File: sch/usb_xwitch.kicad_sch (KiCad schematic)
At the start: 62 parts, among them J1 USB3_A, J2 USB3_A, J3 USB3_A, J4 USB3_A, J5 USB3_A, J6 USB3_A, J7 USB3_A, J8 Conn_02x05_Odd_Even, J9 Conn_02x03_Odd_Even, K1 J104D2C3VDC.15S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

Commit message: updated 3d model and pcb, sch finalize
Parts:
- added D8: VS-10BQ015, Diode_SMD:D_SMB_Handsoldering, symbol Diode:Z2SMBxxx
- added Q3: 2N7002P, Package_TO_SOT_SMD:SOT-23, symbol Transistor_FET:2N7002
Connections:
- net SW-B is gone; now on net REL-B: TP7.1, U1.27 (GPIO21)
- net +5V: now also K3.A1, D8.1 (K)
- net GND: now also K3.11, Q3.2 (S)
- net REL-B: no longer TP6.1, U1.26 (GPIO20)
- net VBUS2: now reaches J5.1 (VBUS), K2.22
- net VBUS2: now also R11.1
- net at J6.1 (VBUS): now also K3.21
- net at J6.2 (D-): now also J7.2 (D-)
- net at J6.3 (D+): now also J7.3 (D+)
- net at J6.5 (SSRX-): now also J7.5 (SSRX-)
- net at J6.6 (SSRX+): now also J7.6 (SSRX+)
- net at J6.8 (SSTX-): now also J7.8 (SSTX-)
- net at J6.9 (SSTX+): now also J7.9 (SSTX+)
- net VBUS3: now reaches J7.1 (VBUS)
- net VBUS3: now also K3.22, R12.1
- net at J7.10 (SHIELD), J7.4 (GND), J7.7 (DRAIN): now also K3.12
- net RL3: now reaches K3.A2
- net RL3: now also D8.2 (A), Q3.3 (D)
- new net REL-C: Q3.1 (G), TP6.1, U1.26 (GPIO20)
- no-connect marks 26 -> 28
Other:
- moved on the sheet: C9, D1, D2, D3, D4, D5, D6, D7, J8, J9, JP1, JP2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

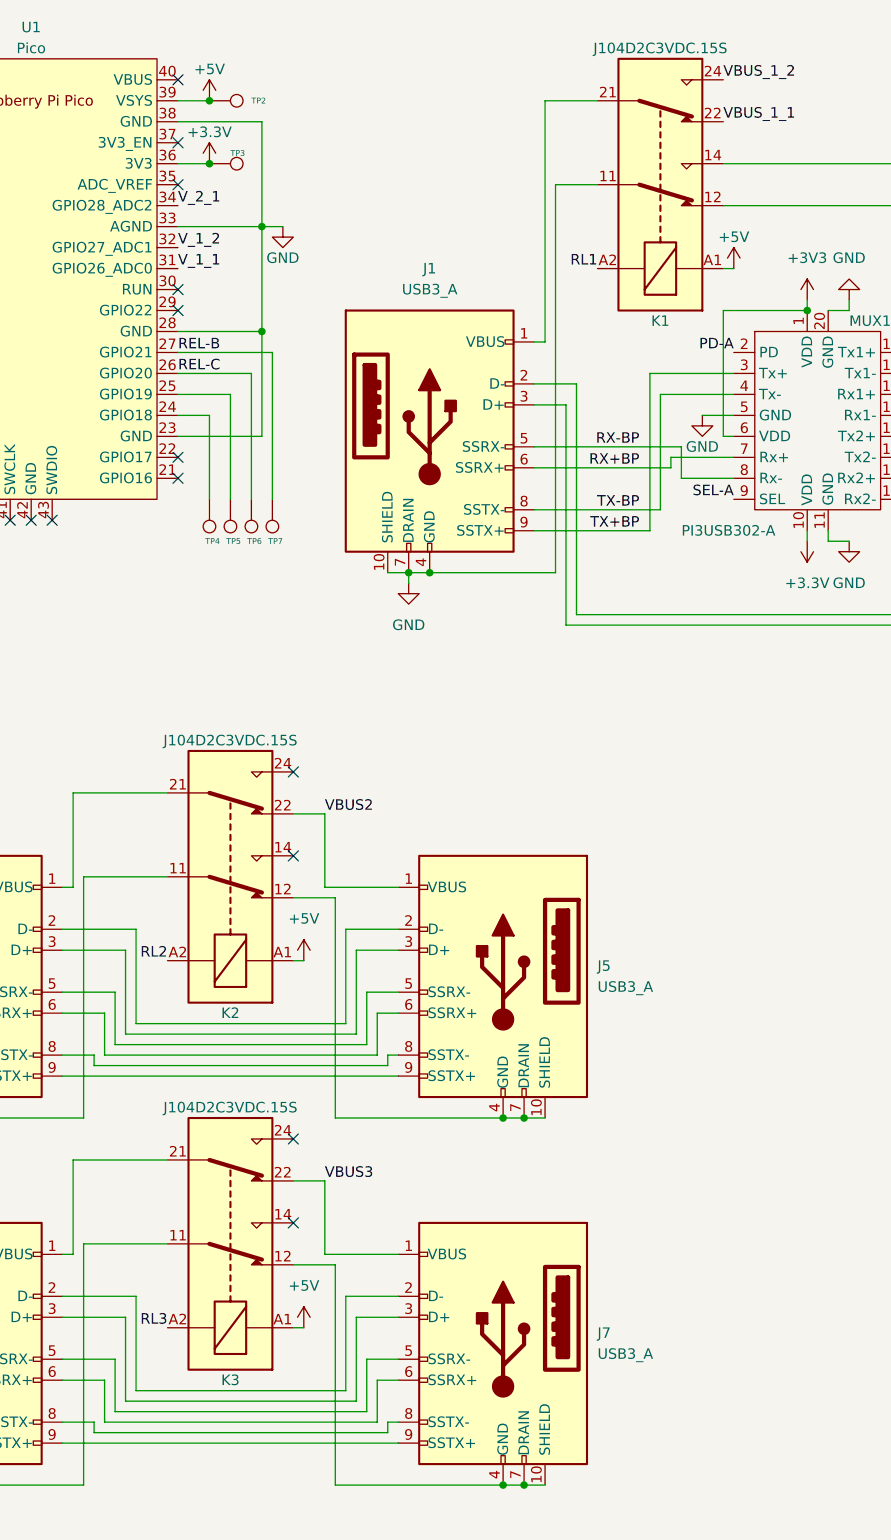
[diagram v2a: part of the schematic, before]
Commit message: updated pcb to 2 sides
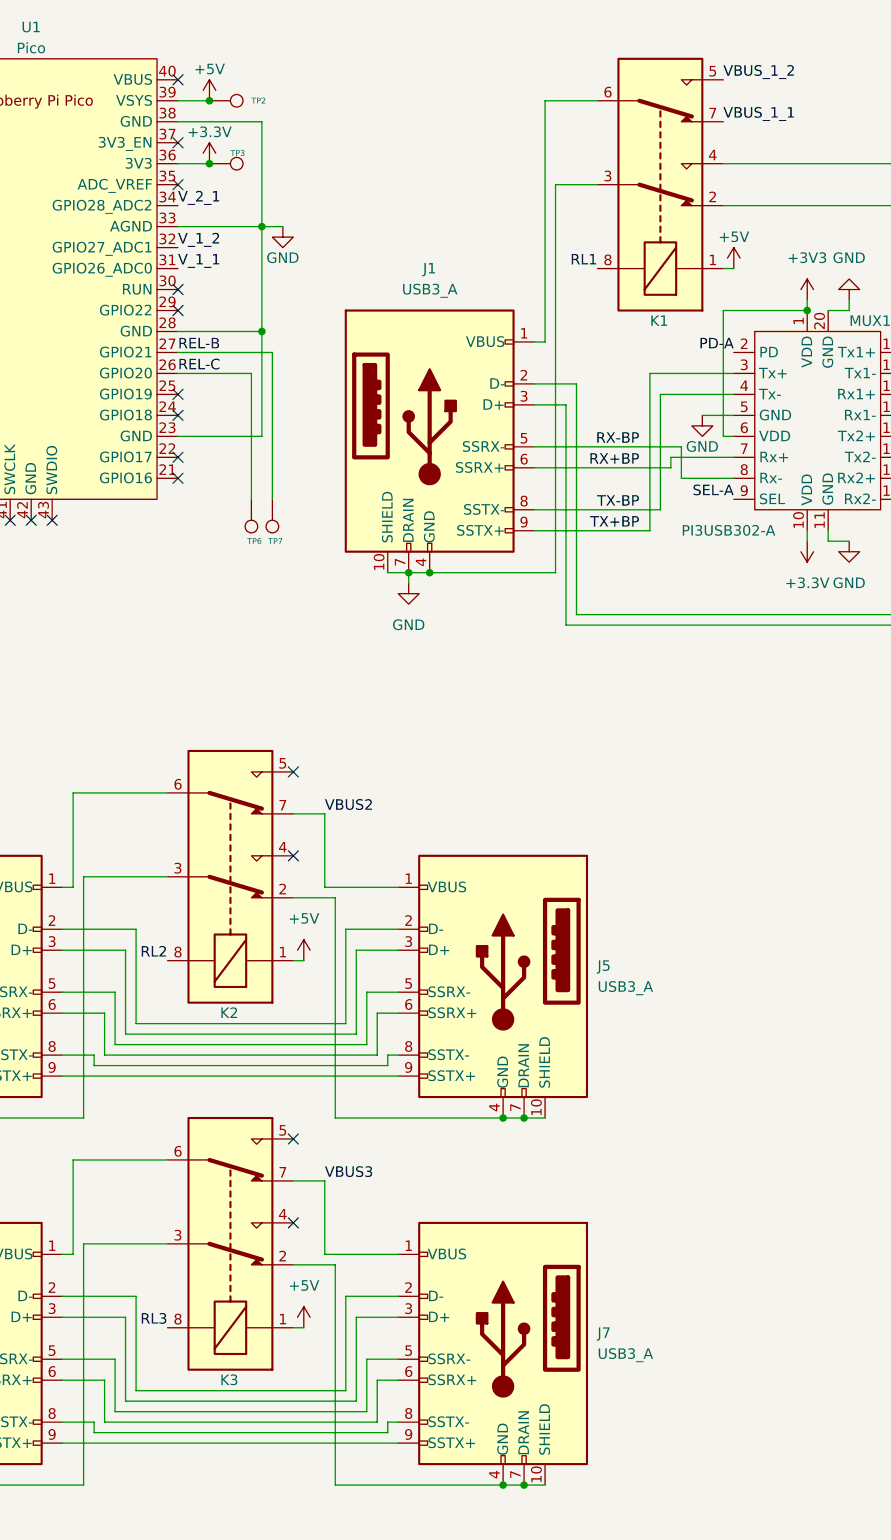
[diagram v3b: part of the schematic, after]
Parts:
- removed TP4, TP5: TestPoint, TestPoint:TestPoint_Pad_D1.0mm, symbol Connector:TestPoint
- C1, C2, C3, C4, C5, C6, C7, C8: footprint Capacitor_SMD:C_1206_3216Metric_Pad1.33x1.80mm_HandSolder -> Capacitor_SMD:C_0805_2012Metric_Pad1.18x1.45mm_HandSolder
- K1, K2, K3: value J104D2C3VDC.15S -> Relay_DPDT_Panasonic_AGQ200A4H; footprint usb_xwitch:J104D2C3VDC.15S -> usb_xwitch:Relay_DPDT_Panasonic_AGQ200A4H; symbol usb_xwitch:J104D2C3VDC.15S -> usb_xwitch:Relay_DPDT_Panasonic_AGQ200A4H
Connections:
- net +5V: now also K1.1, K2.1, K3.1; no longer K1.A1, K2.A1, K3.A1
- net GND: now also K1.3, K2.3, K3.3; no longer K1.11, K2.11, K3.11
- net RL1: now also K1.8; no longer K1.A2
- net RL2: now also K2.8; no longer K2.A2
- net RL3: now also K3.8; no longer K3.A2
- net VBUS2: now also K2.7; no longer K2.22
- net VBUS3: now also K3.7; no longer K3.22
- net VBUS_1_1: now also K1.7; no longer K1.22
- net VBUS_1_2: now also K1.5; no longer K1.24
- net at J5.10 (SHIELD), J5.4 (GND), J5.7 (DRAIN): now also K2.2; no longer K2.12
- net at J4.1 (VBUS): now also K2.6; no longer K2.21
- net at J3.10 (SHIELD), J3.4 (GND), J3.7 (DRAIN): now also K1.4; no longer K1.14
- net at J6.1 (VBUS): now also K3.6; no longer K3.21
- net at J7.10 (SHIELD), J7.4 (GND), J7.7 (DRAIN): now also K3.2; no longer K3.12
- net at J1.1 (VBUS): now also K1.6; no longer K1.21
- net at J2.10 (SHIELD), J2.4 (GND), J2.7 (DRAIN): now also K1.2; no longer K1.12
- no-connect marks 28 -> 30

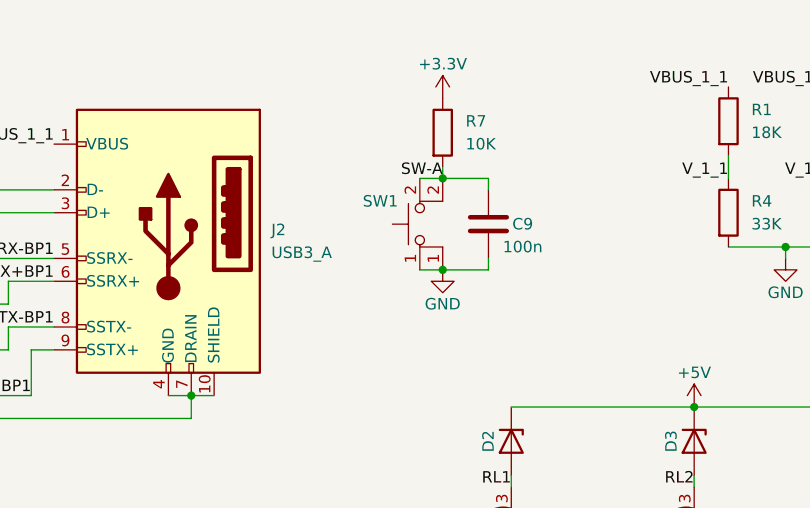
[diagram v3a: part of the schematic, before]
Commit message: all components within rpi hat dimension
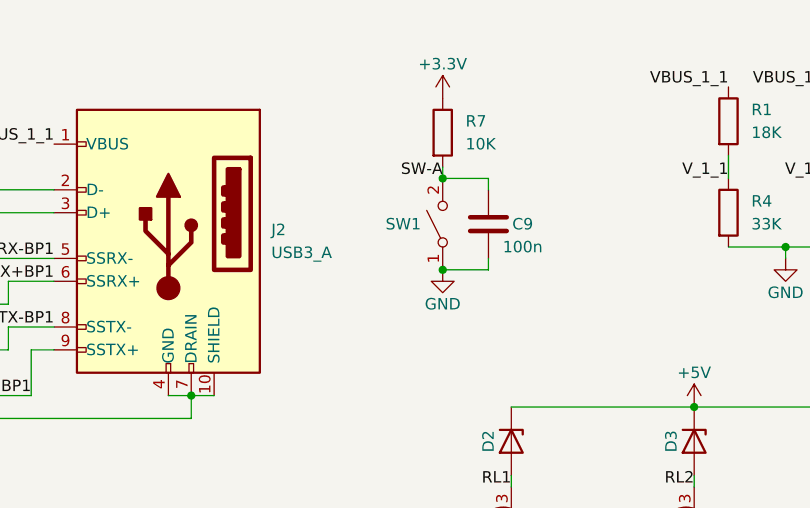
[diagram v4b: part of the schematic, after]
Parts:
- removed SW1: SW_MEC_5E, Button_Switch_THT:SW_PUSH_6mm, symbol Switch:SW_MEC_5E
- added SW1: SW_SPST, usb_xwitch:SW_SPST_CK_PTS636_SP43_SMTR, symbol Switch:SW_SPST
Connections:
- net GND: now also SW1.1 (A)
- net SW-A: now also SW1.2 (B)
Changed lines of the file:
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@@
-    (stroke (width 0) (type default) (color 0 0 0 0))
-  )
-  (wire (pts (xy 217.17 40.64) (xy 219.71 40.64))
     (stroke (width 0) (type default) (color 0 0 0 0))
   )
@@
   )
   (wire (pts (xy 71.12 50.8) (xy 71.12 38.1))
-    (stroke (width 0) (type default) (color 0 0 0 0))
-  )
-  (wire (pts (xy 217.17 30.48) (xy 219.71 30.48))
     (stroke (width 0) (type default) (color 0 0 0 0))
   )
@@
     )
     (property "Datasheet" "~" (id 3) (at 234.95 140.97 0)
+      (effects (font (size 1.27 1.27)) hide)
+    )
+    (pin "1")
+    (pin "2")
+  )
+  (symbol (lib_id "Switch:SW_SPST") (at 219.71 35.56 90) (unit 1)
+    (in_bom yes) (on_board yes)
+    (property "Reference" "SW1" (id 0) (at 213.36 35.56 90)
+      (effects (font (size 1.27 1.27)) (justify right))
+    )
+    (property "Value" "SW_SPST" (id 1) (at 220.98 36.8299 90)
+      (effects (font (size 1.27 1.27)) (justify right) hide)
+    )
+    (property "Footprint" "usb_xwitch:SW_SPST_CK_PTS636_SP43_SMTR" (id 2) (at 219.71 35.56 0)
+      (effects (font (size 1.27 1.27)) hide)
+    )
+    (property "Datasheet" "https://www.ckswitches.com/media/2779/pts636.pdf" (id 3) (at 219.71 35.56 0)
       (effects (font (size 1.27 1.27)) hide)
     )
@@
     (pin "1")
   )
-  (symbol (lib_name "SW_MEC_5E_1") (lib_id "Switch:SW_MEC_5E") (at 219.71 35.56 90) (unit 1)
-    (in_bom yes) (on_board yes)
-    (property "Reference" "SW1" (id 0) (at 210.82 33.02 90)
-      (effects (font (size 1.27 1.27)) (justify right))
-    )
-    (property "Value" "SW_MEC_5E" (id 1) (at 223.52 52.07 90)
-      (effects (font (size 1.27 1.27)) (justify right) hide)
-    )
-    (property "Footprint" "Button_Switch_THT:SW_PUSH_6mm" (id 2) (at 222.25 35.56 0)
-      (effects (font (size 1.27 1.27)) hide)
-    )
-    (property "Datasheet" "" (id 3) (at 220.98 43.18 0)
-      (effects (font (size 1.27 1.27)) hide)
-    )
-    (pin "1")
-    (pin "1")
-    (pin "2")
-    (pin "2")
-  )
   (symbol (lib_id "Connector:TestPoint") (at 21.59 73.66 180) (unit 1)
     (in_bom yes) (on_board yes)
@@
       (reference "R12") (unit 1) (value "402") (footprint "Diode_SMD:D_0201_0603Metric_Pad0.64x0.40mm_HandSolder")
     )
-    (path "/e763556c-3aa8-4eb1-b263-7f108caa2254"
-      (reference "SW1") (unit 1) (value "SW_MEC_5E") (footprint "Button_Switch_THT:SW_PUSH_6mm")
+    (path "/af047df2-64d9-4941-aac1-dbe0147cb1ee"
+      (reference "SW1") (unit 1) (value "SW_SPST") (footprint "usb_xwitch:SW_SPST_CK_PTS636_SP43_SMTR")
     )
     (path "/d0028305-0b95-450c-8359-16b71d14c347"

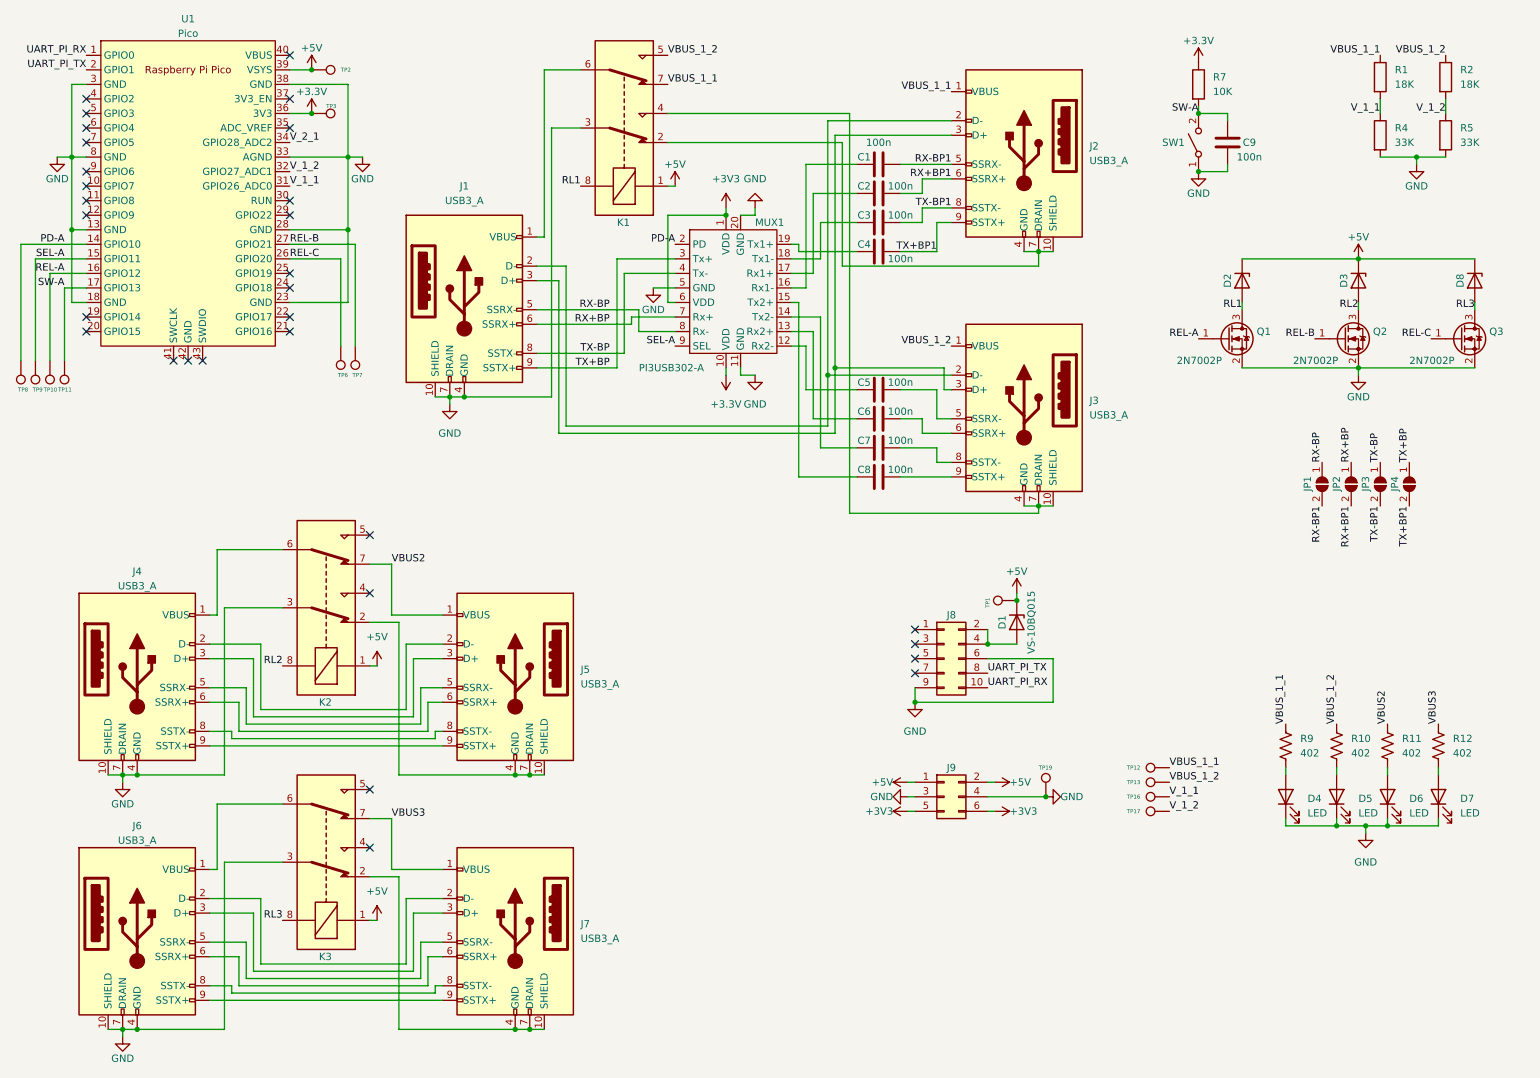
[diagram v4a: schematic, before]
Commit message: usb gnd changed; wired mux1 all parts
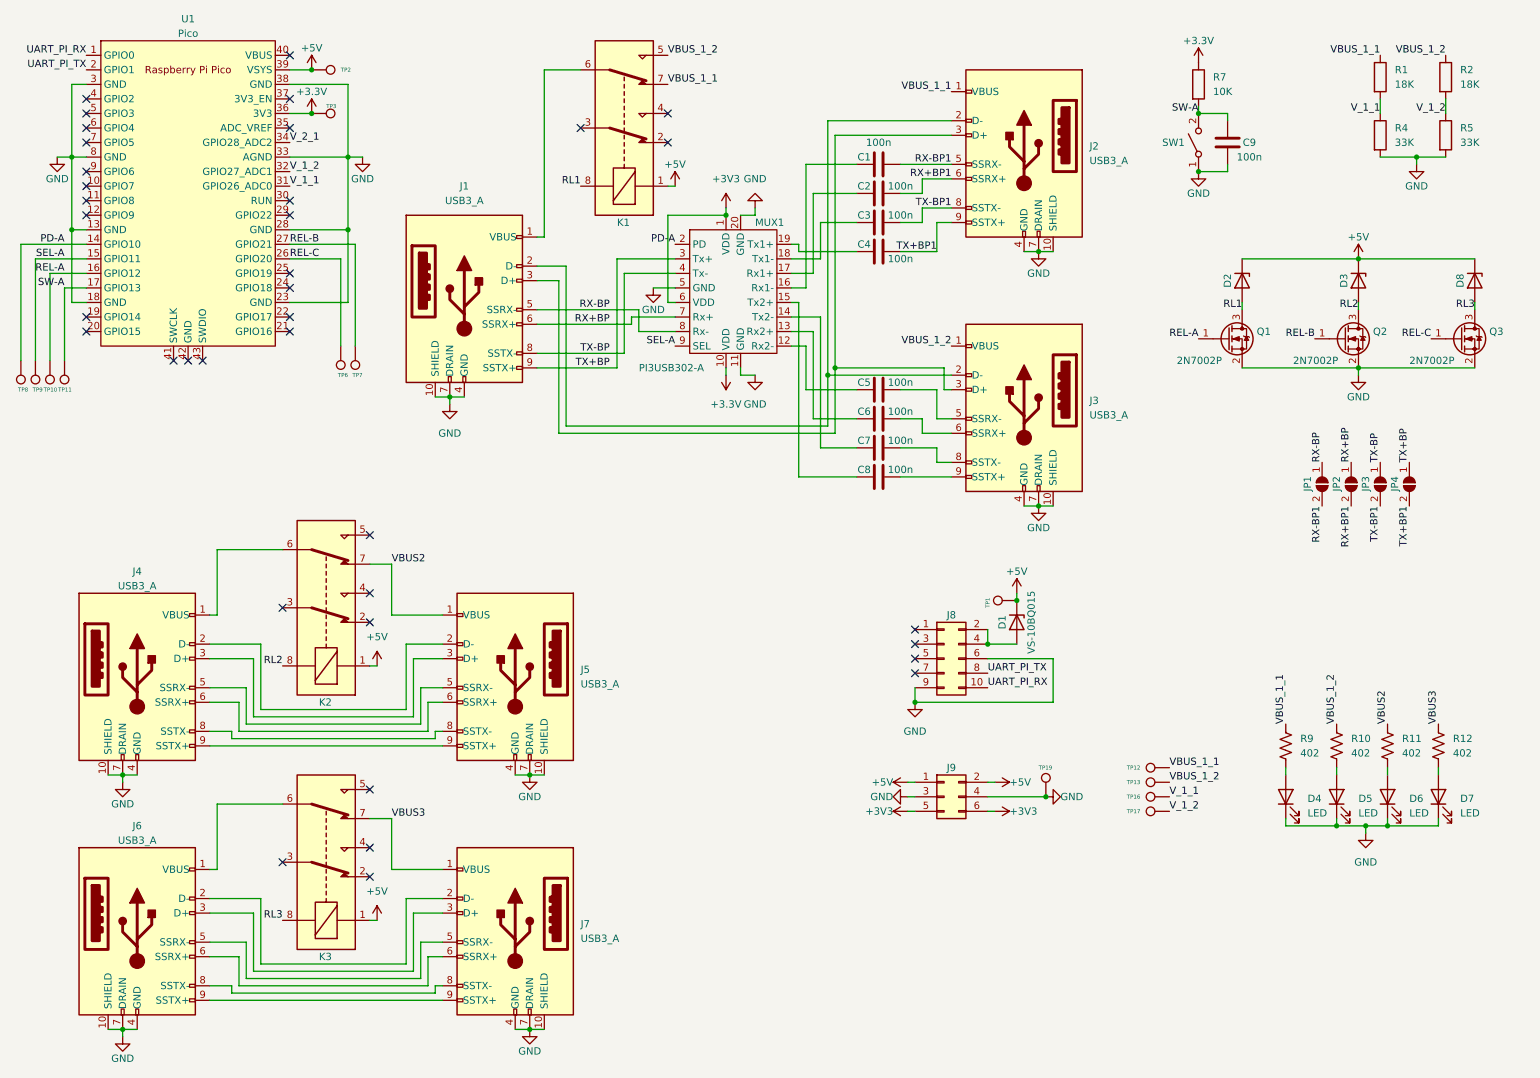
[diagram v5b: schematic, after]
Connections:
- net GND: now also J2.10 (SHIELD), J2.4 (GND), J2.7 (DRAIN), J3.10 (SHIELD), J3.4 (GND), J3.7 (DRAIN), J5.10 (SHIELD), J5.4 (GND), J5.7 (DRAIN), J7.10 (SHIELD), J7.4 (GND), J7.7 (DRAIN); no longer K1.3, K2.3, K3.3
- now unconnected: K1.2, K1.4, K2.2, K3.2
- no-connect marks 30 -> 37

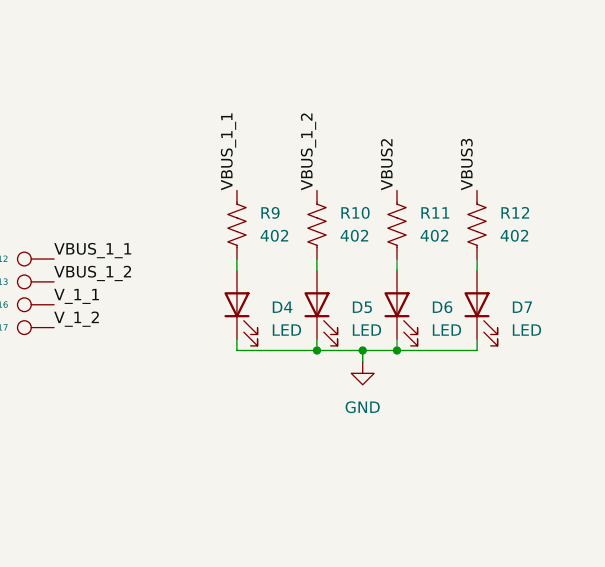
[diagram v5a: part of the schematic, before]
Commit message: led, res, sw, j footprint changed for manufacture
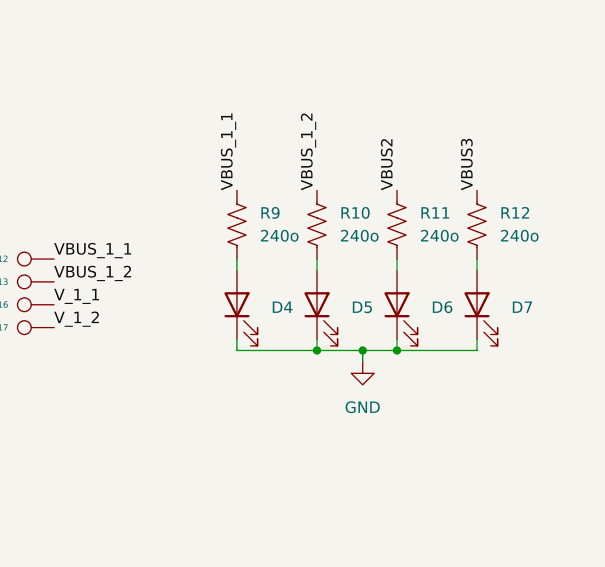
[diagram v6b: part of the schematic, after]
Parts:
- D4, D5, D6, D7: value LED -> 19-217/GHC-YR1S2/3T; footprint Diode_SMD:D_0201_0603Metric_Pad0.64x0.40mm_HandSolder -> Diode_SMD:D_0603_1608Metric_Pad1.05x0.95mm_HandSolder
- J9: value Conn_02x03_Odd_Even -> C65114Copy; footprint Connector_PinHeader_2.00mm:PinHeader_2x03_P2.00mm_Vertical -> Connector_PinHeader_2.54mm:PinHeader_2x03_P2.54mm_Vertical
- R10, R11, R12, R9: value 402 -> 240o; footprint Diode_SMD:D_0201_0603Metric_Pad0.64x0.40mm_HandSolder -> Resistor_SMD:R_0603_1608Metric_Pad0.98x0.95mm_HandSolder
- SW1: value SW_SPST -> C2689642
